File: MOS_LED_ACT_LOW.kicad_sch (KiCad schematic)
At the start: 5 parts, among them Q3 FDV304P

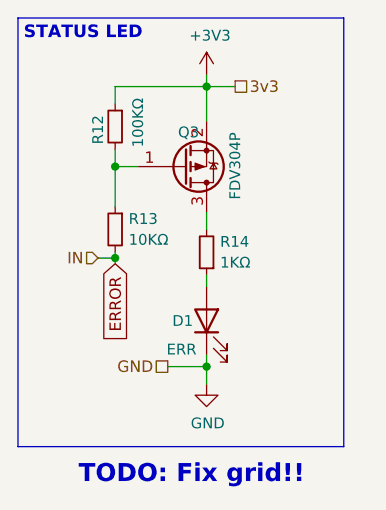
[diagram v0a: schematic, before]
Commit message: Latest revision - dc protection and change to wrover
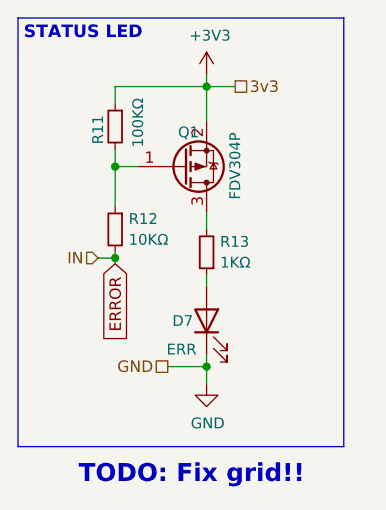
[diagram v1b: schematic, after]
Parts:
- renumbered D1 to D7, Q3 to Q1, R12 to R11, R13 to R12, R14 to R13
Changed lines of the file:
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@@
   (symbol (lib_id "Device:Q_PMOS_GSD") (at 161.29 90.805 0) (mirror x) (unit 1)
     (in_bom yes) (on_board yes)
-    (property "Reference" "Q3" (id 0) (at 160.655 86.995 0)
+    (property "Reference" "Q1" (id 0) (at 160.655 86.995 0)
       (effects (font (size 1.2 1.2)) (justify left))
     )
@@
   (symbol (lib_id "Device:R_Small") (at 153.67 97.79 0) (mirror y) (unit 1)
     (in_bom yes) (on_board yes)
-    (property "Reference" "R13" (id 0) (at 155.1686 96.6216 0)
+    (property "Reference" "R12" (id 0) (at 155.1686 96.6216 0)
       (effects (font (size 1.2 1.2)) (justify right))
     )
@@
   (symbol (lib_id "Device:LED") (at 163.83 107.95 90) (unit 1)
     (in_bom yes) (on_board yes)
-    (property "Reference" "D1" (id 0) (at 160.02 107.95 90)
+    (property "Reference" "D7" (id 0) (at 160.02 107.95 90)
       (effects (font (size 1.2 1.2)) (justify right))
     )
@@
   (symbol (lib_id "power:+3V3") (at 163.83 80.645 0) (unit 1)
     (in_bom yes) (on_board yes)
-    (property "Reference" "#PWR0153" (id 0) (at 163.83 84.455 0)
+    (property "Reference" "#PWR042" (id 0) (at 163.83 84.455 0)
       (effects (font (size 1.2 1.2)) hide)
     )
@@
   (symbol (lib_id "Device:R_Small") (at 163.83 100.33 180) (unit 1)
     (in_bom yes) (on_board yes)
-    (property "Reference" "R14" (id 0) (at 165.3286 99.1616 0)
+    (property "Reference" "R13" (id 0) (at 165.3286 99.1616 0)
       (effects (font (size 1.2 1.2)) (justify right))
     )
@@
   (symbol (lib_id "Device:R_Small") (at 153.67 86.36 0) (mirror y) (unit 1)
     (in_bom yes) (on_board yes)
-    (property "Reference" "R12" (id 0) (at 151.765 85.09 90)
+    (property "Reference" "R11" (id 0) (at 151.765 85.09 90)
       (effects (font (size 1.2 1.2)) (justify right))
     )
@@
   (symbol (lib_id "power:GND") (at 163.83 114.935 0) (unit 1)
     (in_bom yes) (on_board yes)
-    (property "Reference" "#PWR0167" (id 0) (at 163.83 121.285 0)
+    (property "Reference" "#PWR043" (id 0) (at 163.83 121.285 0)
       (effects (font (size 1.2 1.2)) hide)
     )
